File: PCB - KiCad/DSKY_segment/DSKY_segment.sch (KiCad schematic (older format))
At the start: 3 parts, among them J1 Conn_15X4, J2 Conn_15X4, J3 Conn_15X4

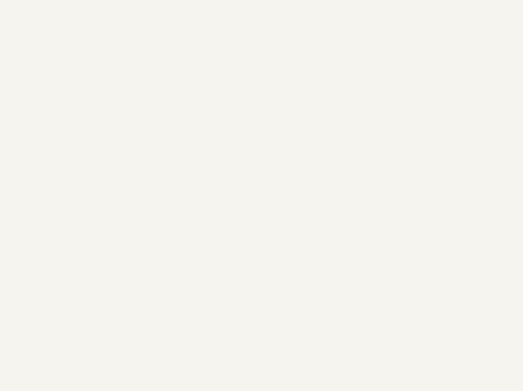
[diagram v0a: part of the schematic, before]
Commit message: V3 of PCB hardware
3.3 to 5V level shifter added
Added decoupling caps to 5V rail and HV rail
Added cap to RESET line
Fixed locating holes in FX6 footprint
Fixed unintentional trace overlap
Eliminated the "GND" feature, and re-assigned all lines to be the common electrode
Fixed a routing error on the segment PCB, and re-assigned one common electrode line to be a segment line.
The above changes mean that the common electrode mask in firmware *must* be updated.
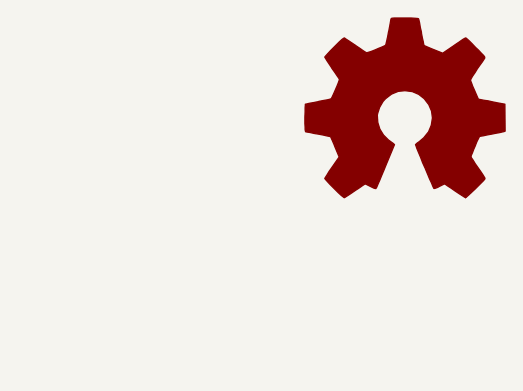
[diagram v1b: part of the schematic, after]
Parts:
- added LOGO1: Logo_Open_Hardware_Large, Symbol:OSHW-Logo2_7.3x6mm_SilkScreen, symbol Graphic:Logo_Open_Hardware_Large
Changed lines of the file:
@@
 EESchema Schematic File Version 4
+LIBS:DSKY_segment-cache
 EELAYER 29 0
 EELAYER END
@@
 	1    0    0    -1
 $EndComp
+$Comp
+L Graphic:Logo_Open_Hardware_Large LOGO1
+U 1 1 5CBD35AE
+P 10000 1300
+F 0 "LOGO1" H 10000 1800 50  0001 C CNN
+F 1 "Logo_Open_Hardware_Large" H 10000 900 50  0001 C CNN
+F 2 "Symbol:OSHW-Logo2_7.3x6mm_SilkScreen" H 10000 1300 50  0001 C CNN
+F 3 "~" H 10000 1300 50  0001 C CNN
+	1    10000 1300
+	1    0    0    -1
+$EndComp

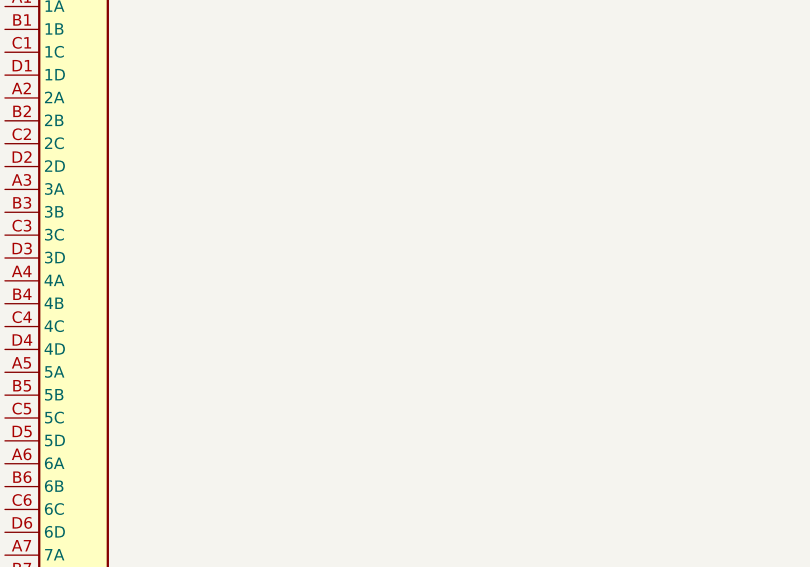
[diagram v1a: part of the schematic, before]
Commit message: V4 of segment PCB
Routing fixes.  Added protection diode for common electrode
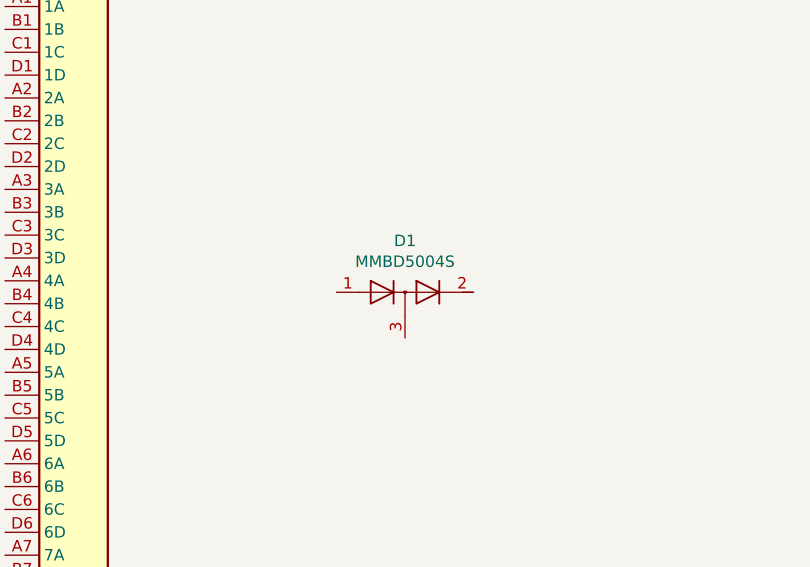
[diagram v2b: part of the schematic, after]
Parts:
- added D1: MMBD5004S, Package_TO_SOT_SMD:SOT-23, symbol DSKY_driver:MMBD5004S
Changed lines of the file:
@@
+	1    0    0    -1
+$EndComp
+$Comp
+L DSKY_driver:MMBD5004S D1
+U 1 1 5CD013B2
+P 5650 2250
+F 0 "D1" H 5650 2475 50  0000 C CNN
+F 1 "MMBD5004S" H 5650 2384 50  0000 C CNN
+F 2 "Package_TO_SOT_SMD:SOT-23" H 5650 2250 50  0001 C CNN
+F 3 "" H 5650 2250 50  0001 C CNN
+	1    5650 2250
 	1    0    0    -1
 $EndComp

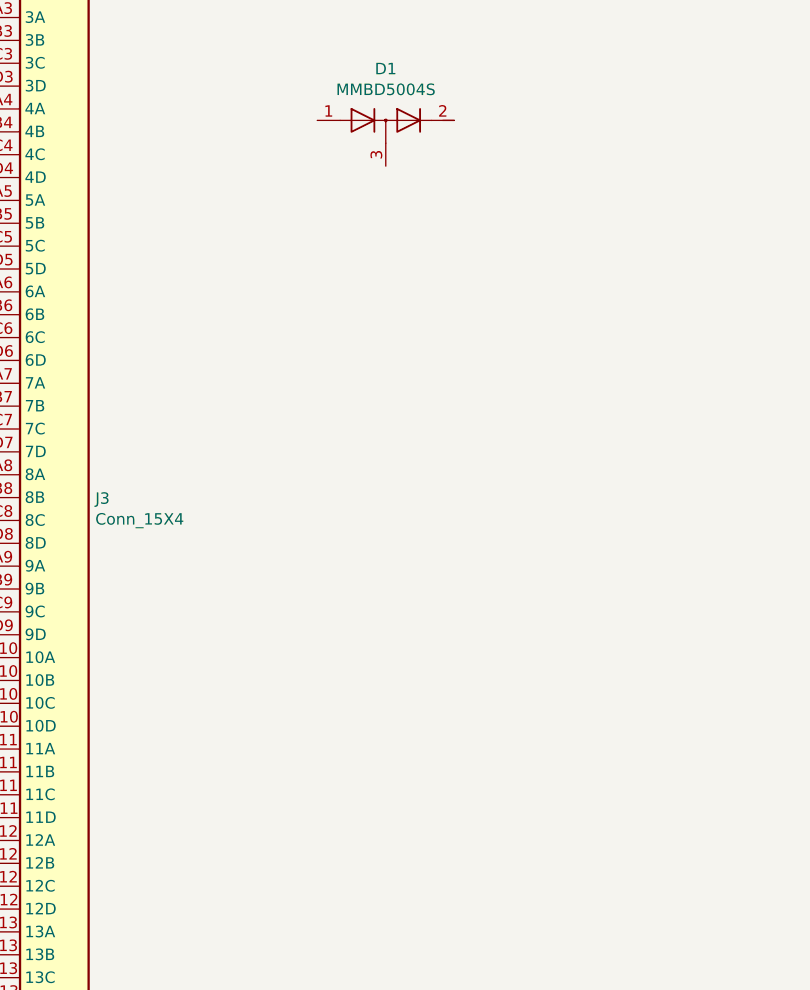
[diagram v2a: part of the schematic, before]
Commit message: Add 0402 size current limiting resistors. Update PCB markings
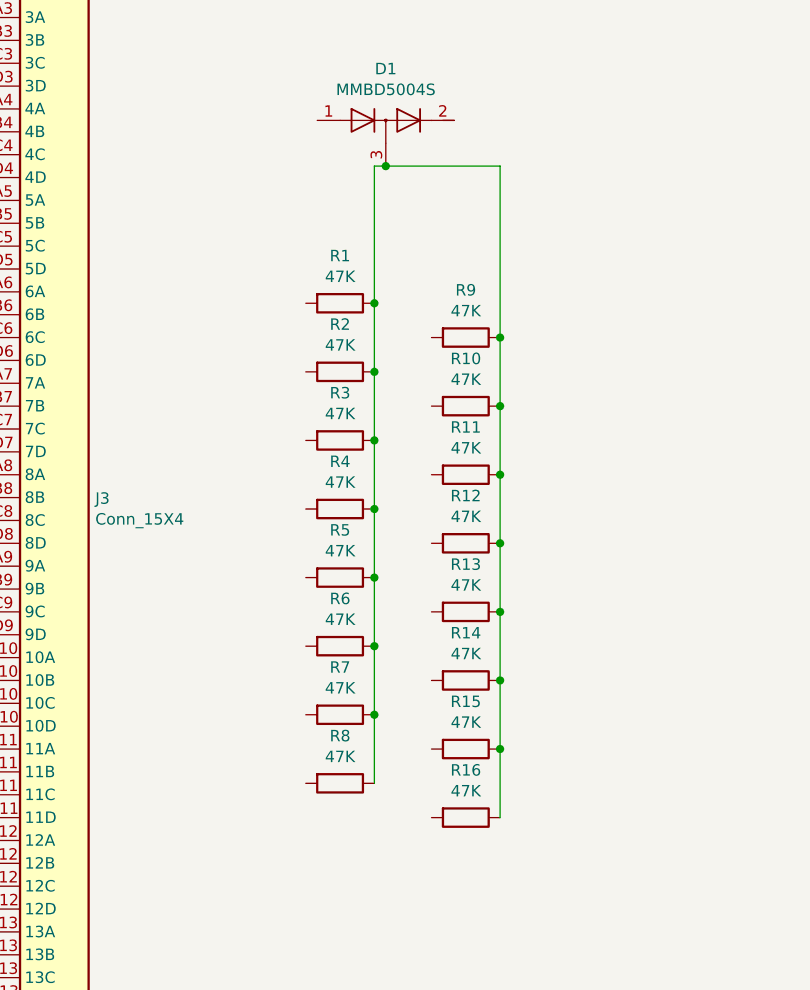
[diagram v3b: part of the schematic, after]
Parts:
- added R1, R10, R11, R12, R13, R14, R15, R16, R2, R3, R4, R5, R6, R7, R8, R9: 47K, Resistor_SMD:R_0402_1005Metric, symbol Device:R
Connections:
- net at D1.3: now also R1.1, R10.1, R11.1, R12.1, R13.1, R14.1, R15.1, R16.1, R2.1, R3.1, R4.1, R5.1, R6.1, R7.1, R8.1, R9.1
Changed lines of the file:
@@
 EESchema Schematic File Version 4
-LIBS:DSKY_segment-cache
-EELAYER 29 0
+EELAYER 30 0
 EELAYER END
 $Descr A4 11693 8268
@@
 	1    0    0    -1
 $EndComp
+$Comp
+L Device:R R1
+U 1 1 5F049CFB
+P 5450 3050
+F 0 "R1" V 5243 3050 50  0000 C CNN
+F 1 "47K" V 5334 3050 50  0000 C CNN
+F 2 "Resistor_SMD:R_0402_1005Metric" V 5380 3050 50  0001 C CNN
+F 3 "~" H 5450 3050 50  0001 C CNN
+	1    5450 3050
+	0    1    1    0
+$EndComp
+$Comp
+L Device:R R2
+U 1 1 5F04B080
+P 5450 3350
+F 0 "R2" V 5243 3350 50  0000 C CNN
+F 1 "47K" V 5334 3350 50  0000 C CNN
+F 2 "Resistor_SMD:R_0402_1005Metric" V 5380 3350 50  0001 C CNN
+F 3 "~" H 5450 3350 50  0001 C CNN
+	1    5450 3350
+	0    1    1    0
+$EndComp
+$Comp
+L Device:R R3
+U 1 1 5F04BB75
+P 5450 3650
+F 0 "R3" V 5243 3650 50  0000 C CNN
+F 1 "47K" V 5334 3650 50  0000 C CNN
+F 2 "Resistor_SMD:R_0402_1005Metric" V 5380 3650 50  0001 C CNN
+F 3 "~" H 5450 3650 50  0001 C CNN
+	1    5450 3650
+	0    1    1    0
+$EndComp
+$Comp
+L Device:R R4
+U 1 1 5F04C447
+P 5450 3950
+F 0 "R4" V 5243 3950 50  0000 C CNN
+F 1 "47K" V 5334 3950 50  0000 C CNN
+F 2 "Resistor_SMD:R_0402_1005Metric" V 5380 3950 50  0001 C CNN
+F 3 "~" H 5450 3950 50  0001 C CNN
+	1    5450 3950
+	0    1    1    0
+$EndComp
+$Comp
+L Device:R R5
+U 1 1 5F04F613
+P 5450 4250
+F 0 "R5" V 5243 4250 50  0000 C CNN
+F 1 "47K" V 5334 4250 50  0000 C CNN
+F 2 "Resistor_SMD:R_0402_1005Metric" V 5380 4250 50  0001 C CNN
+F 3 "~" H 5450 4250 50  0001 C CNN
+	1    5450 4250
+	0    1    1    0
+$EndComp
+$Comp
+L Device:R R6
+U 1 1 5F04F61D
+P 5450 4550
+F 0 "R6" V 5243 4550 50  0000 C CNN
+F 1 "47K" V 5334 4550 50  0000 C CNN
+F 2 "Resistor_SMD:R_0402_1005Metric" V 5380 4550 50  0001 C CNN
+F 3 "~" H 5450 4550 50  0001 C CNN
+	1    5450 4550
+	0    1    1    0
+$EndComp
+$Comp
+L Device:R R7
+U 1 1 5F04F627
+P 5450 4850
+F 0 "R7" V 5243 4850 50  0000 C CNN
+F 1 "47K" V 5334 4850 50  0000 C CNN
+F 2 "Resistor_SMD:R_0402_1005Metric" V 5380 4850 50  0001 C CNN
+F 3 "~" H 5450 4850 50  0001 C CNN
+	1    5450 4850
+	0    1    1    0
+$EndComp
+$Comp
+L Device:R R8
+U 1 1 5F04F631
+P 5450 5150
+F 0 "R8" V 5243 5150 50  0000 C CNN
+F 1 "47K" V 5334 5150 50  0000 C CNN
+F 2 "Resistor_SMD:R_0402_1005Metric" V 5380 5150 50  0001 C CNN
+F 3 "~" H 5450 5150 50  0001 C CNN
+	1    5450 5150
+	0    1    1    0
+$EndComp
+$Comp
+L Device:R R9
+U 1 1 5F054E47
+P 6000 3200
+F 0 "R9" V 5793 3200 50  0000 C CNN
+F 1 "47K" V 5884 3200 50  0000 C CNN
+F 2 "Resistor_SMD:R_0402_1005Metric" V 5930 3200 50  0001 C CNN
+F 3 "~" H 6000 3200 50  0001 C CNN
+	1    6000 3200
+	0    1    1    0
+$EndComp
+$Comp
+L Device:R R10
+U 1 1 5F054E51
+P 6000 3500
+F 0 "R10" V 5793 3500 50  0000 C CNN
+F 1 "47K" V 5884 3500 50  0000 C CNN
+F 2 "Resistor_SMD:R_0402_1005Metric" V 5930 3500 50  0001 C CNN
+F 3 "~" H 6000 3500 50  0001 C CNN
+	1    6000 3500
+	0    1    1    0
+$EndComp
+$Comp
+L Device:R R11
+U 1 1 5F054E5B
+P 6000 3800
+F 0 "R11" V 5793 3800 50  0000 C CNN
+F 1 "47K" V 5884 3800 50  0000 C CNN
+F 2 "Resistor_SMD:R_0402_1005Metric" V 5930 3800 50  0001 C CNN
+F 3 "~" H 6000 3800 50  0001 C CNN
+	1    6000 3800
+	0    1    1    0
+$EndComp
+$Comp
+L Device:R R12
+U 1 1 5F054E65
+P 6000 4100
+F 0 "R12" V 5793 4100 50  0000 C CNN
+F 1 "47K" V 5884 4100 50  0000 C CNN
+F 2 "Resistor_SMD:R_0402_1005Metric" V 5930 4100 50  0001 C CNN
+F 3 "~" H 6000 4100 50  0001 C CNN
+	1    6000 4100
+	0    1    1    0
+$EndComp
+$Comp
+L Device:R R13
+U 1 1 5F054E6F
+P 6000 4400
+F 0 "R13" V 5793 4400 50  0000 C CNN
+F 1 "47K" V 5884 4400 50  0000 C CNN
+F 2 "Resistor_SMD:R_0402_1005Metric" V 5930 4400 50  0001 C CNN
+F 3 "~" H 6000 4400 50  0001 C CNN
+	1    6000 4400
+	0    1    1    0
+$EndComp
+$Comp
+L Device:R R14
+U 1 1 5F054E79
+P 6000 4700
+F 0 "R14" V 5793 4700 50  0000 C CNN
+F 1 "47K" V 5884 4700 50  0000 C CNN
+F 2 "Resistor_SMD:R_0402_1005Metric" V 5930 4700 50  0001 C CNN
+F 3 "~" H 6000 4700 50  0001 C CNN
+	1    6000 4700
+	0    1    1    0
+$EndComp
+$Comp
+L Device:R R15
+U 1 1 5F054E83
+P 6000 5000
+F 0 "R15" V 5793 5000 50  0000 C CNN
+F 1 "47K" V 5884 5000 50  0000 C CNN
+F 2 "Resistor_SMD:R_0402_1005Metric" V 5930 5000 50  0001 C CNN
+F 3 "~" H 6000 5000 50  0001 C CNN
+	1    6000 5000
+	0    1    1    0
+$EndComp
+$Comp
+L Device:R R16
+U 1 1 5F054E8D
+P 6000 5300
+F 0 "R16" V 5793 5300 50  0000 C CNN
+F 1 "47K" V 5884 5300 50  0000 C CNN
+F 2 "Resistor_SMD:R_0402_1005Metric" V 5930 5300 50  0001 C CNN
+F 3 "~" H 6000 5300 50  0001 C CNN
+	1    6000 5300
+	0    1    1    0
+$EndComp
+Wire Wire Line
+	5600 3050 5600 3350
+Connection ~ 5600 3350
+Wire Wire Line
+	5600 3350 5600 3650
+Connection ~ 5600 3650
+Wire Wire Line
+	5600 3650 5600 3950
+Connection ~ 5600 3950
+Wire Wire Line
+	5600 3950 5600 4250
+Connection ~ 5600 4250
+Wire Wire Line
+	5600 4250 5600 4550
+Connection ~ 5600 4550
+Wire Wire Line
+	5600 4550 5600 4850
+Connection ~ 5600 4850
+Wire Wire Line
+	5600 4850 5600 5150
+Connection ~ 6150 3500
+Wire Wire Line
+	6150 3500 6150 3800
+Connection ~ 6150 3800
+Wire Wire Line
+	6150 3800 6150 4100
+Connection ~ 6150 4100
+Wire Wire Line
+	6150 4100 6150 4400
+Connection ~ 6150 4400
+Wire Wire Line
+	6150 4400 6150 4700
+Connection ~ 6150 4700
+Wire Wire Line
+	6150 4700 6150 5000
+Connection ~ 6150 5000
+Wire Wire Line
+	6150 5000 6150 5300
+Wire Wire Line
+	6150 2450 5650 2450
+Wire Wire Line
+	6150 2450 6150 3200
+Connection ~ 6150 3200
+Wire Wire Line
+	6150 3200 6150 3500
+Wire Wire Line
+	5600 3050 5600 2450
+Wire Wire Line
+	5600 2450 5650 2450
+Connection ~ 5600 3050
+Connection ~ 5650 2450
 $EndSCHEMATC
